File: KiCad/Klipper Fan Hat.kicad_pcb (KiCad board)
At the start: 2 copper layers, 65 x 56 mm, 60 parts, among them J1 GPIO, J2 Serial, J3 I2C, J4 1 Wire, J5 SPI, J6 Vin, Q1 IRLML6344, Q2 IRLML6344, Q3 IRLML6344, Q4 IRLML6344, Q5 IRLML6344, T0 Thermistor, T1 Thermistor, U1 CAT24C256

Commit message: Rename to Klipper Fan Hat
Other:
- board text added: "Klipper Fan Hat Created by Michael Thomas"
- board text removed: "Klipper Expander Hat Created by Michael Thomas"

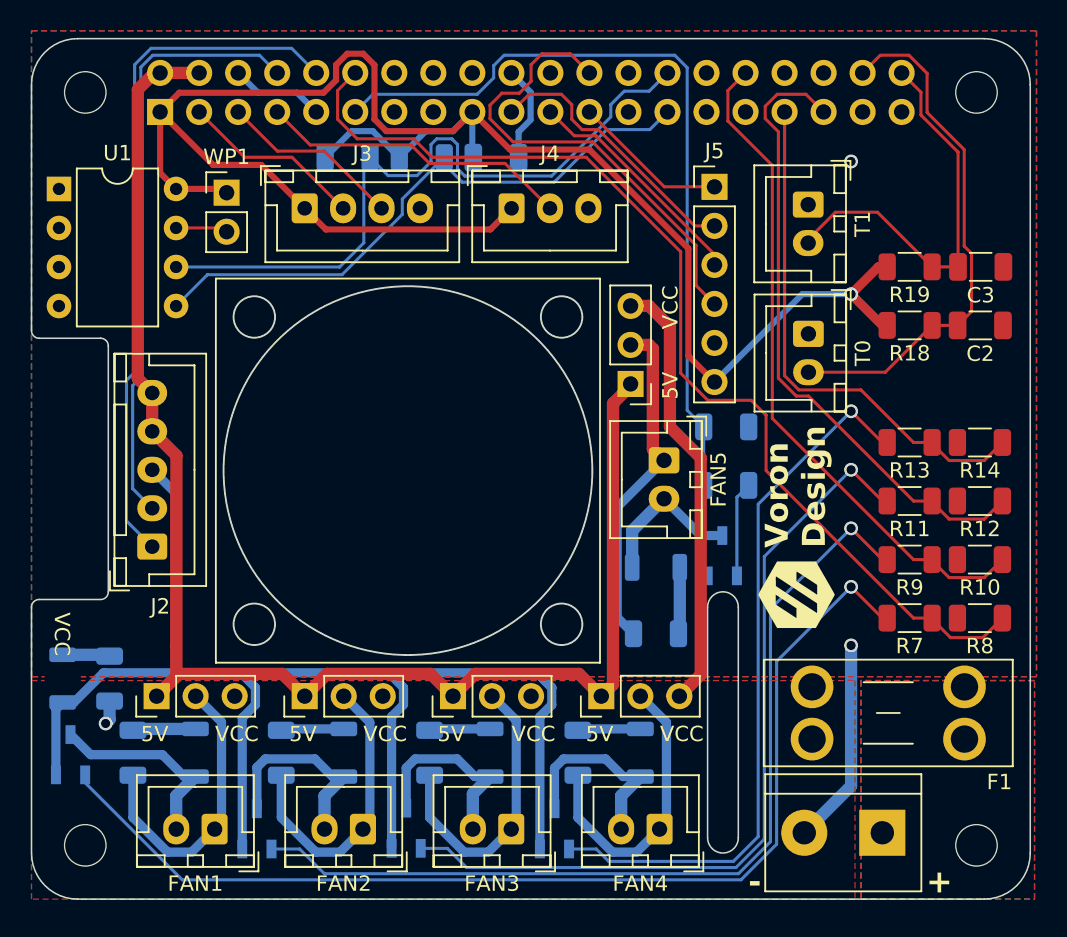
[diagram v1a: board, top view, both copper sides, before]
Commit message: Update Klipper Fan Hat to V2
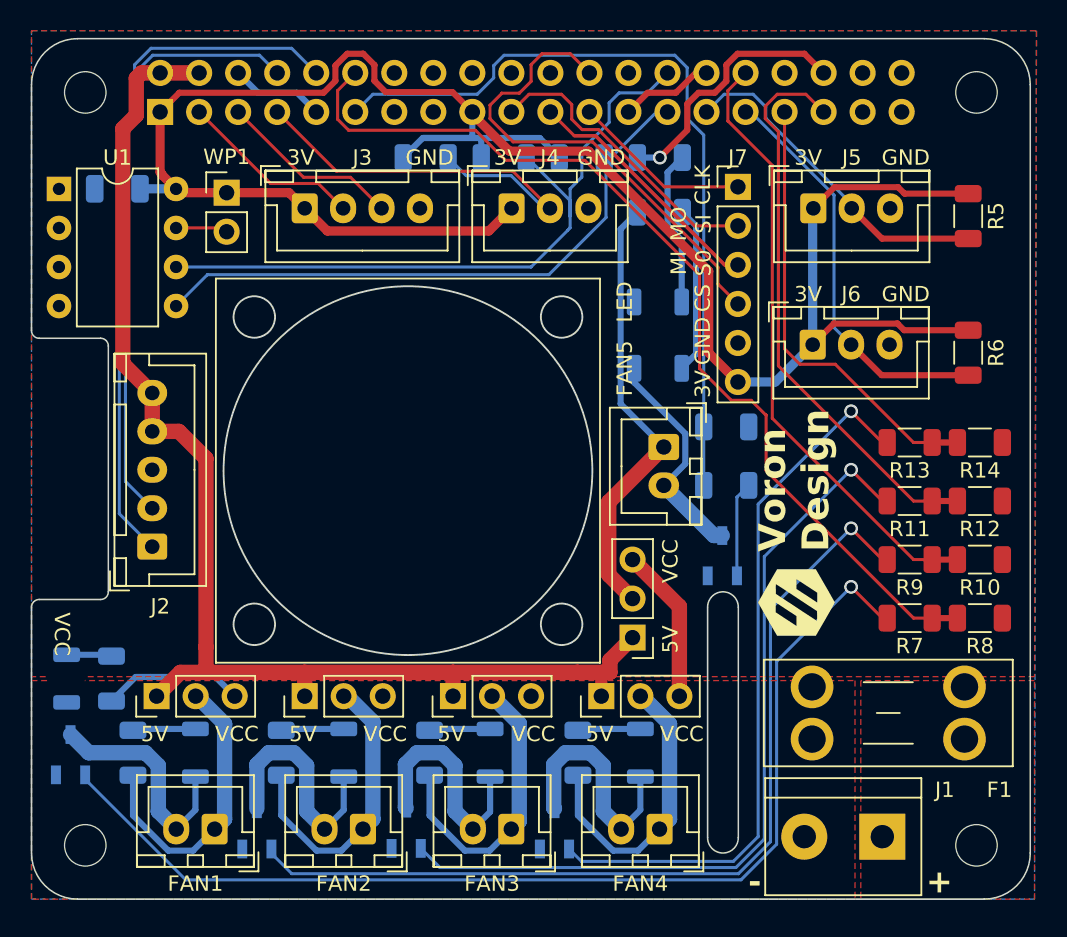
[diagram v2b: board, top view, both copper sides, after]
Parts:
- removed C2, C3: 4.7uF, Capacitor_SMD:C_1206_3216Metric
- removed the R18 at (157.2, 62.7)
- removed the R19 at (157.2, 58.9)
- removed the R20 at (105.1, 85.6)
- removed T0, T1: Thermistor, Connector_JST:JST_XH_B2B-XH-A_1x02_P2.50mm_Vertical
- added D7: LED, LED_SMD:LED_1206_3216Metric_ReverseMount_Hole1.8x2.4mm, B.Cu at (102.3, 85.6)
- added J1: Vin, TerminalBlock:TerminalBlock_bornier-2_P5.08mm, F.Cu at (155.4, 95.9)
- added J5: GPIO5, Connector_JST:JST_XH_B3B-XH-A_1x03_P2.50mm_Vertical, F.Cu at (150.9, 55.0)
- added R1: 1k, Resistor_SMD:R_1206_3216Metric, B.Cu at (140.9, 51.7)
- added R22: 4.7k, Resistor_SMD:R_1206_3216Metric, B.Cu at (105.2, 85.6)
- added R4: 3.9k, Resistor_SMD:R_1206_3216Metric, B.Cu at (125.7, 51.7)
- added R5: 3.9k, Resistor_SMD:R_1206_3216Metric, F.Cu at (161.0, 55.5)
- added R6: 3.9k, Resistor_SMD:R_1206_3216Metric, F.Cu at (161.0, 64.4)
- J6: value Vin -> GPIO6; footprint TerminalBlock:TerminalBlock_bornier-2_P5.08mm -> Connector_JST:JST_XH_B3B-XH-A_1x03_P2.50mm_Vertical
- moved D6 45.8 mm to (140.8, 61.1), turned to 0 degrees
- moved J6 32.1 mm to (150.8, 63.9), turned to 0 degrees
- moved R21 27.4 mm to (140.9, 55.3)
- moved C1 24.7 mm to (105.6, 53.8)
- moved JP5 16.5 mm to (139.1, 83.0)
- moved D5 13.0 mm to (140.8, 65.5)
- moved R2 10.4 mm to (135.8, 51.7)
- moved R3 10.2 mm to (130.7, 51.7)
- moved J7 1.52 mm to (146.0, 53.6)
- moved FAN5 0.87 mm to (141.1, 70.6)
- moved G*** 0.51 mm to (149.8, 80.7)
- renumbered J5 to J7, J1 to J8, R16 to R15, R17 to R16, R3 to R17, R4 to R18, R5 to R19, R1 to R2, R6 to R20, R15 to R21, R2 to R3
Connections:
- C1 pad 1: +3V3 -> GND
- C1 pad 2: GND -> +3V3
- F1 pad 2: Net-(J6-Pin_1) -> Net-(J1-Pin_1)
- J6 pad 1: Net-(J6-Pin_1) -> +3V3
- J6 pad 2: GND -> /GPIO6
- R10 pad 1: /GPIO12/PWM0 -> GND
- R10 pad 2: GND -> /GPIO12/PWM0
- R12 pad 1: /GPIO19/PCM.FS -> GND
- R12 pad 2: GND -> /GPIO19/PCM.FS
- R14 pad 1: /GPIO13/PWM1 -> GND
- R14 pad 2: GND -> /GPIO13/PWM1
- R8 pad 1: /GPIO18/PCM.CLK -> GND
- R8 pad 2: GND -> /GPIO18/PCM.CLK
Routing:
- net GND: track 114.3 -> 12.3 mm, vias 2 -> 0
- net /GPIO20/PCM.DIN: track 34.1 -> 0.00 mm
- net /GPIO6: track 0.00 -> 26.6 mm
- net /GPIO21/PCM.DOUT: track 26.3 -> 0.00 mm
- net /GPIO5: track 0.00 -> 22.0 mm
- net /GPIO16: track 0.00 -> 17.1 mm, vias 0 -> 1
- net +3V3: track 122.5 -> 138.2 mm, vias 1 -> 0
- net +5V: track 99.1 -> 84.2 mm
- net /GPIO9/SPI0.MISO: track 15.2 -> 29.6 mm
- net VCC: track 30.6 -> 19.3 mm, vias 1 -> 0
- net /GPIO4/GPCLK0: track 20.3 -> 28.3 mm
- net Net-(D6-A): track 3.08 -> 10.2 mm
- net Net-(FAN5-Pin_1): track 22.1 -> 28.9 mm
- net Net-(D5-A): track 4.35 -> 10.9 mm
- net /GPIO18/PCM.CLK: track 68.0 -> 63.0 mm
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- added copper zone on F.Cu, net Net-(J1-Pin_1)
- removed copper zone on B.Cu, net Net-(J6-Pin_1)
- removed copper zone on F.Cu, net Net-(J6-Pin_1)
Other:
- board text added: "3V"
- board text added: "CLK"
- board text added: "CS"
- board text added: "GND"
- board text added: "LED"
- board text added: "MI S0"
- board text added: "MO SI"
- board text added: "RX"
- board text added: "TX"
- board text added: "V2"

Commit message: Update Klipper Fan Hat software to V2
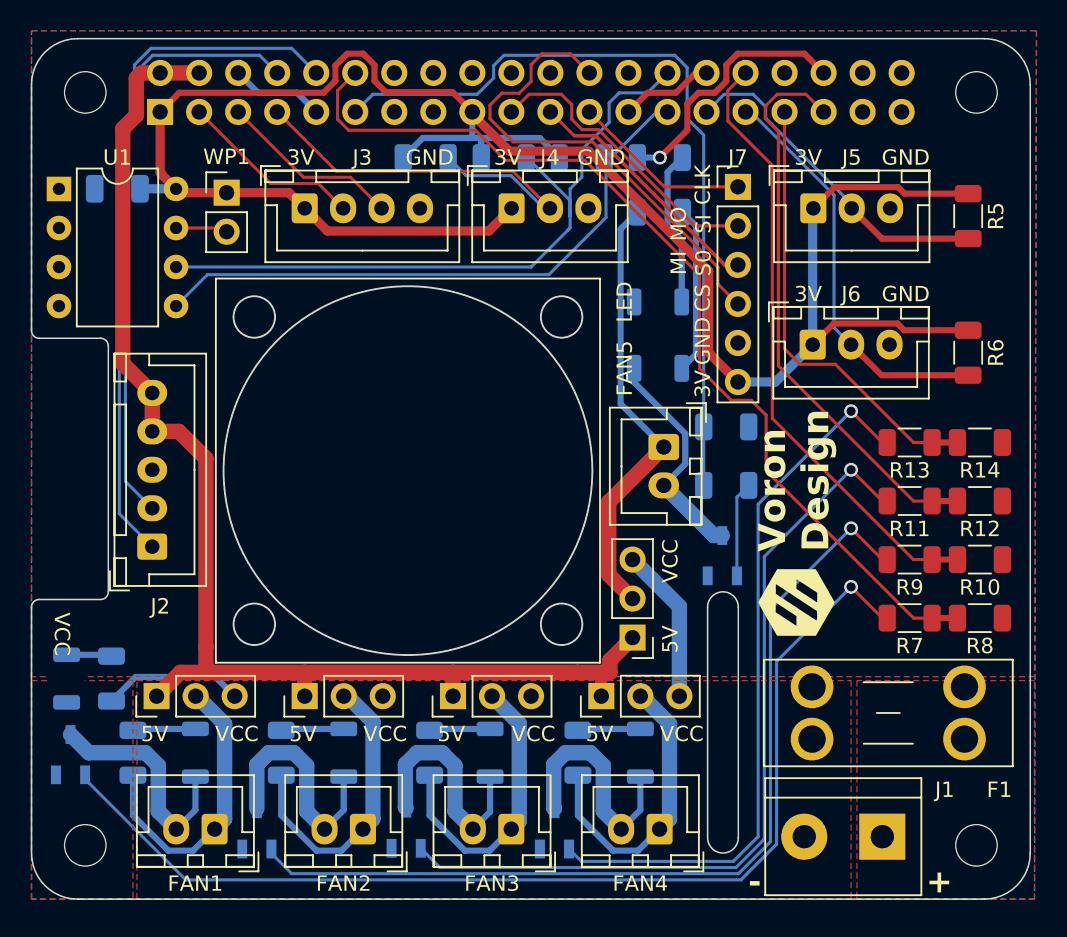
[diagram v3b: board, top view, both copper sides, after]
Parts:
- added G***: LOGO, LOGO, B.Cu at (155.8, 87.9)
